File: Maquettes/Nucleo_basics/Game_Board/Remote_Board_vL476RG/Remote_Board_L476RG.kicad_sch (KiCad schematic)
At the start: 46 parts, among them CON1 MikroE-nRF-S-module, J1 LCD_SD, J10 3.3V_reg, J11 V_Ecl_1, J2 JoyStick, J3 AnalogIn, J4 BAT_IN, J5 Morpho_Gauche, J6 Morpho_Droite, J7 V_ECLAIRAGE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

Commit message: Update Remote L476RG
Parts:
- removed C1: 10nF, symbol Device:C
- removed J11: V_Ecl_1, TerminalBlock:TerminalBlock_bornier-2_P5.08mm, symbol Connector_Generic:Conn_01x02
- removed J7: V_ECLAIRAGE, TerminalBlock_Phoenix:TerminalBlock_Phoenix_MKDS-3-2-5.08_1x02_P5.08mm_Horizontal, symbol Connector_Generic:Conn_01x02
- removed Q1: IRL540N, Package_TO_SOT_THT:TO-220-3_Vertical, symbol Transistor_FET:IRF540N
- removed R1: 8.2k, symbol Device:R
- removed R10: 8.2k, Resistor_THT:R_Axial_DIN0207_L6.3mm_D2.5mm_P10.16mm_Horizontal, symbol Device:R
- added C6: 10nF, Capacitor_THT:C_Rect_L7.0mm_W3.5mm_P5.00mm, symbol Device:C
- added R16: 8.2k, Resistor_THT:R_Axial_DIN0207_L6.3mm_D2.5mm_P10.16mm_Horizontal, symbol Device:R
- added SW5: SW_5, LEnsE_devices:Switch, symbol Switch:SW_Push
- C2, C3, C4, C5: footprint (none) -> Capacitor_THT:C_Rect_L7.0mm_W3.5mm_P5.00mm
- CON1: footprint MIKROBUS_MODULE_CONN -> miKro:MIKROBUS_MODULE_CONN
- D3, D4, D5, D6, D7: footprint (none) -> LED_THT:LED_D3.0mm_Clear
- J1: footprint (none) -> Connector_PinSocket_2.54mm:PinSocket_1x11_P2.54mm_Horizontal
- J2: footprint (none) -> Connector_PinSocket_2.54mm:PinSocket_1x05_P2.54mm_Horizontal
- J8: footprint (none) -> Connector_PinSocket_2.54mm:PinSocket_1x04_P2.54mm_Horizontal
- R11, R12, R13, R14, R15, R2, R3, R5, R6, R7, R8, R9: footprint (none) -> Resistor_THT:R_Axial_DIN0207_L6.3mm_D2.5mm_P10.16mm_Horizontal
- SW2, SW3, SW4: footprint (none) -> LEnsE_devices:Switch
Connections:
- net 3.3V_NUC: now also C6.1, SW5.1
- net GND: now also R16.2
- net SW1_OUT: now also J6.20 (Pin_20); no longer J6.14 (Pin_14)
- net SW2_OUT: now also J6.18 (Pin_18); no longer J6.16 (Pin_16)
- net SW3_OUT: now also J6.16 (Pin_16); no longer J6.18 (Pin_18)
- net SW4_OUT: now also J6.14 (Pin_14); no longer J6.20 (Pin_20)
- net SW5_OUT: now reaches J6.8 (Pin_8)
- net SW5_OUT: now also C6.2, R16.1, SW5.2
- no-connect marks 14 -> 16

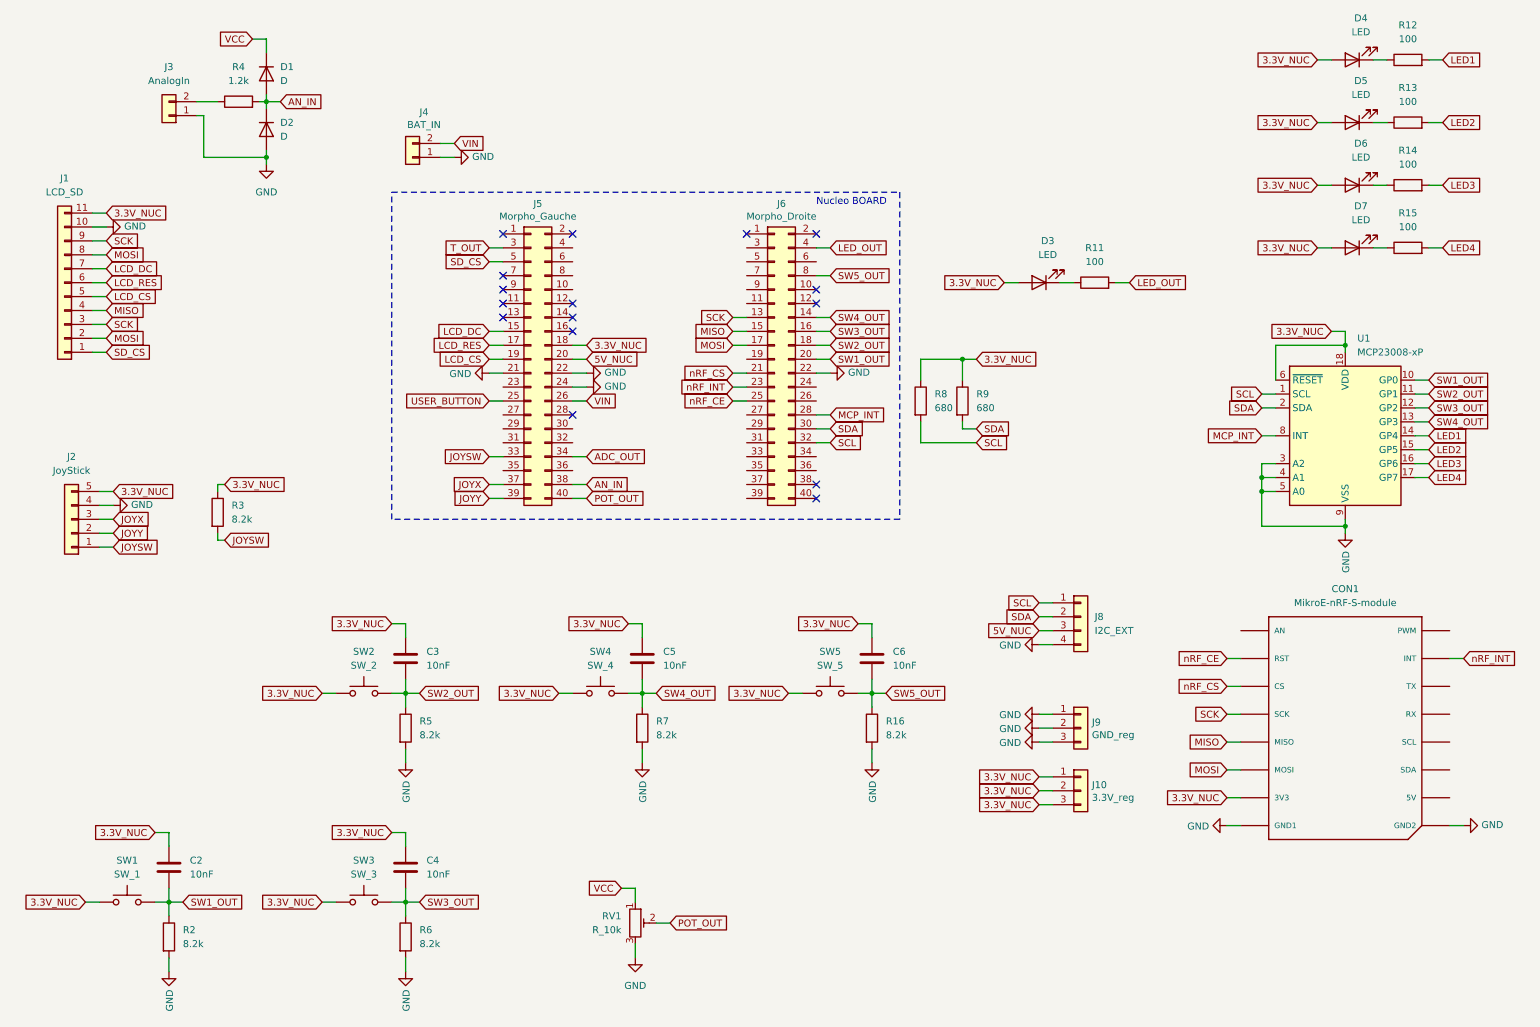
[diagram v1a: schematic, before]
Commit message: Update Remote Board / L476RG version
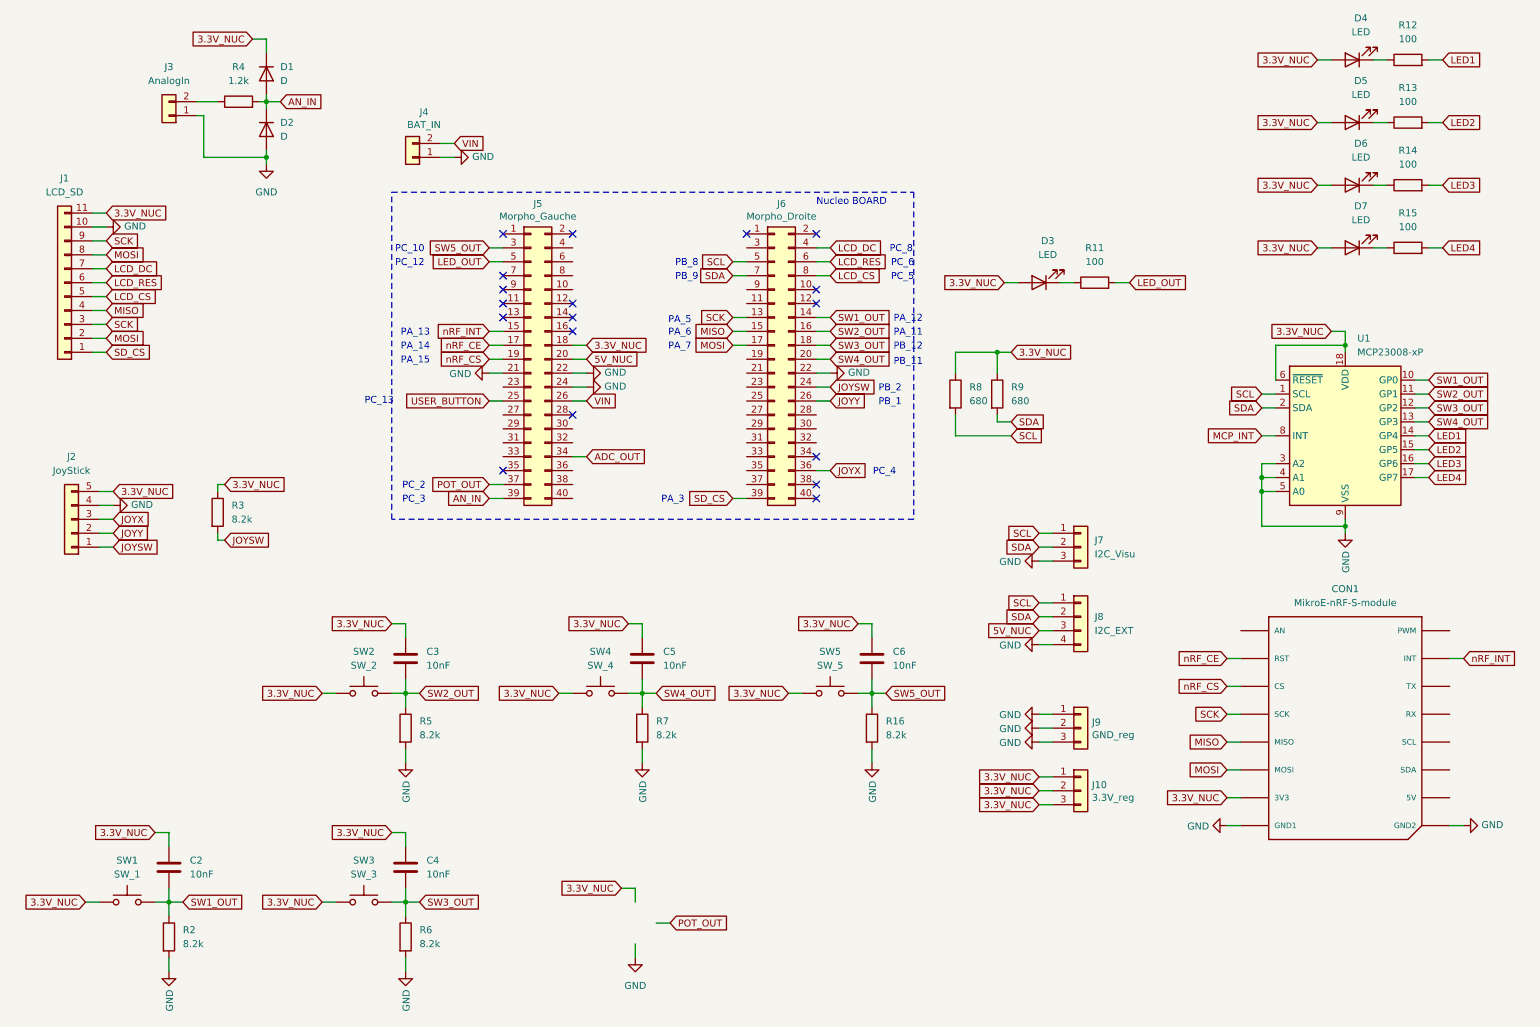
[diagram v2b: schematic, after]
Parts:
- removed RV1: R_10k, Potentiometer_THT:Potentiometer_Vishay_T73YP_Vertical, symbol Device:R_POT_TRIM
- added J7: I2C_Visu, Connector_PinSocket_2.54mm:PinSocket_1x03_P2.54mm_Vertical, symbol Connector_Generic:Conn_01x03
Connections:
- net T_OUT is gone; now on net SW5_OUT: J5.3 (Pin_3)
- net VCC is gone; now on net 3.3V_NUC: D1.1 (K)
- net AN_IN: now also J5.39 (Pin_39); no longer J5.38 (Pin_38)
- net GND: now also J7.3 (Pin_3)
- net JOYSW: now also J6.24 (Pin_24); no longer J5.33 (Pin_33)
- net JOYX: now also J6.36 (Pin_36); no longer J5.37 (Pin_37)
- net JOYY: now also J6.26 (Pin_26); no longer J5.39 (Pin_39)
- net LCD_CS: now also J6.8 (Pin_8); no longer J5.19 (Pin_19)
- net LCD_DC: now also J6.4 (Pin_4); no longer J5.15 (Pin_15)
- net LCD_RES: now also J6.6 (Pin_6); no longer J5.17 (Pin_17)
- net LED_OUT: now also J5.5 (Pin_5); no longer J6.4 (Pin_4)
- net MCP_INT: no longer J6.28 (Pin_28)
- net POT_OUT: now also J5.37 (Pin_37); no longer J5.40 (Pin_40)
- net SCL: now also J6.5 (Pin_5), J7.1 (Pin_1); no longer J6.32 (Pin_32)
- net SDA: now also J6.7 (Pin_7), J7.2 (Pin_2); no longer J6.30 (Pin_30)
- net SD_CS: now also J6.39 (Pin_39); no longer J5.5 (Pin_5)
- net SW1_OUT: now also J6.14 (Pin_14); no longer J6.20 (Pin_20)
- net SW2_OUT: now also J6.16 (Pin_16); no longer J6.18 (Pin_18)
- net SW3_OUT: now also J6.18 (Pin_18); no longer J6.16 (Pin_16)
- net SW4_OUT: now also J6.20 (Pin_20); no longer J6.14 (Pin_14)
- net SW5_OUT: no longer J6.8 (Pin_8)
- net nRF_CE: now also J5.17 (Pin_17); no longer J6.25 (Pin_25)
- net nRF_CS: now also J5.19 (Pin_19); no longer J6.21 (Pin_21)
- net nRF_INT: now also J5.15 (Pin_15); no longer J6.23 (Pin_23)
- no-connect marks 16 -> 18
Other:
- note added: "PA_11"
- note added: "PA_12"
- note added: "PA_13"
- note added: "PA_14"
- note added: "PA_15"
- note added: "PA_3"
- note added: "PA_5"
- note added: "PA_6"
- note added: "PA_7"
- note added: "PB_1"
- note added: "PB_11"
- note added: "PB_12"
- note added: "PB_2"
- note added: "PB_8"
- note added: "PB_9"
- note added: "PC_10"
- note added: "PC_12"
- note added: "PC_13"
- note added: "PC_2"
- note added: "PC_3"
- note added: "PC_4"
- note added: "PC_5"
- note added: "PC_6"
- note added: "PC_8"
- moved on the sheet: R8, R9

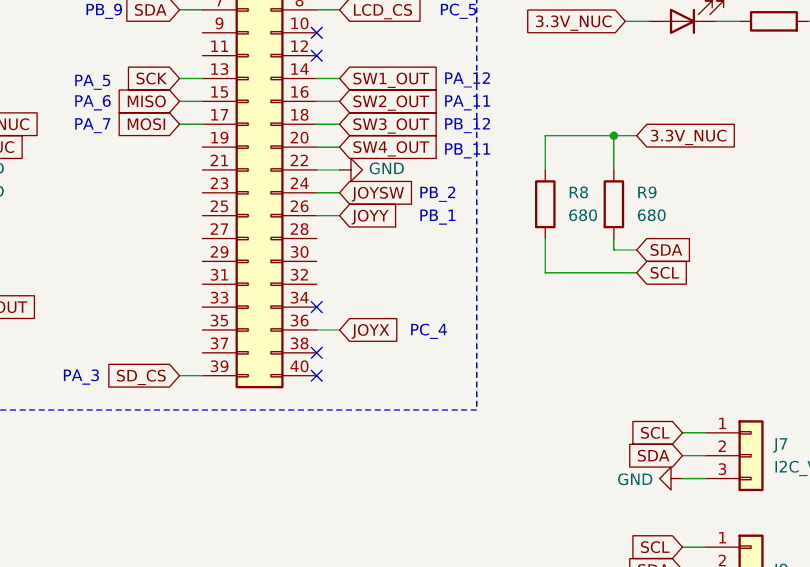
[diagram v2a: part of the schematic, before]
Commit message: Update Remote Board / L476RG
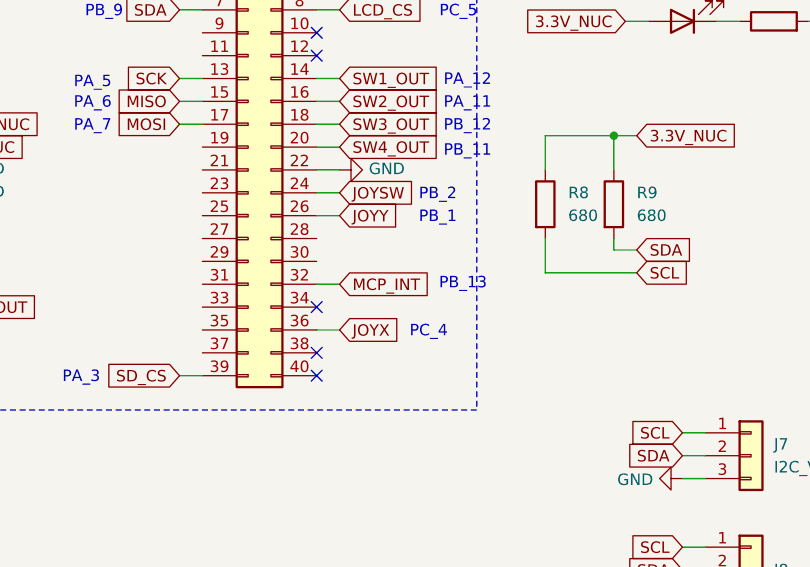
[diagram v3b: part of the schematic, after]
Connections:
- net MCP_INT: now also J6.32 (Pin_32)
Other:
- note added: "PB_13"
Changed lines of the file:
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@@
 	(wire
 		(pts
+			(xy 156.21 91.44) (xy 158.75 91.44)
+		)
+		(stroke
+			(width 0)
+			(type default)
+		)
+	)
+	(wire
+		(pts
 			(xy 55.88 29.21) (xy 58.42 29.21)
 		)
@@
 		)
 	)
+	(text "PB_13"
+		(exclude_from_sim no)
+		(at 172.466 91.44 0)
+		(effects
+			(font
+				(size 1.27 1.27)
+			)
+		)
+	)
 	(text "PA_14"
 		(exclude_from_sim no)
@@
 			(effects
 				(font
+					(size 1.27 1.27)
+				)
+				(hide yes)
+			)
+		)
+	)
+	(global_label "MCP_INT"
+		(shape input)
+		(at 158.75 91.44 0)
+		(effects
+			(font
+				(size 1.27 1.27)
+			)
+			(justify left)
+		)
+		(property "Intersheetrefs" "${INTERSHEET_REFS}"
+			(at 158.75 91.44 0)
+			(effects
+				(font
